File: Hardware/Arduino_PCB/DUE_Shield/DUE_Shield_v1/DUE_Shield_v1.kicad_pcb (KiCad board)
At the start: 2 copper layers, 101.6 x 62 mm, 34 parts, among them J1 SPI_Header, J2 Conn_02x05_Counter_Clockwise, J3 Reset_+_Dos, J4 V_Supply, J5 Main_Con, J6 Motor_PWM, J7 Audio, J8 Display_Con, J9 Erweiterungs_Con, P1 Digital, P2 Power, P3 Analog, P4 Analog, P5 PWM, P6 PWM, P7 Communication, U1 SD_Karte_Attend

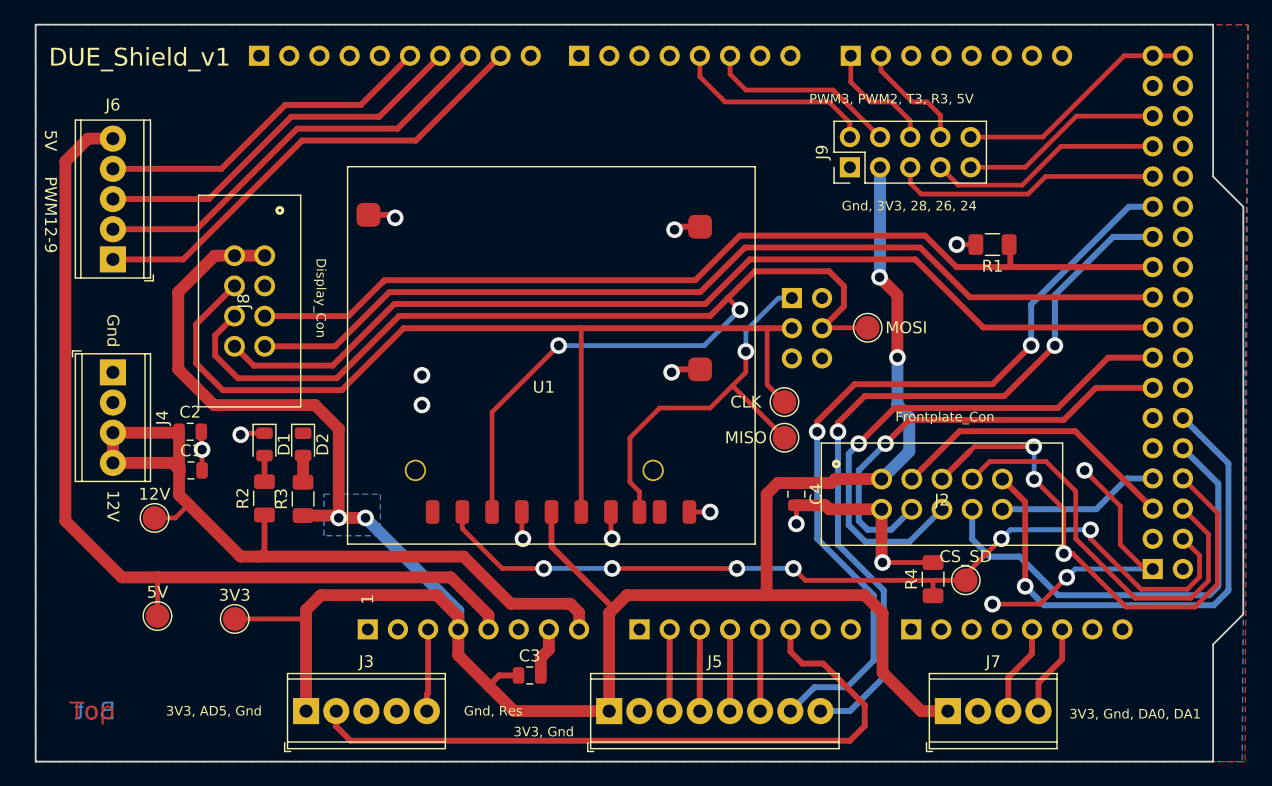
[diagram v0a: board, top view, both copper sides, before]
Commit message: Update DUE_Shield inkl. 3d-Modelle
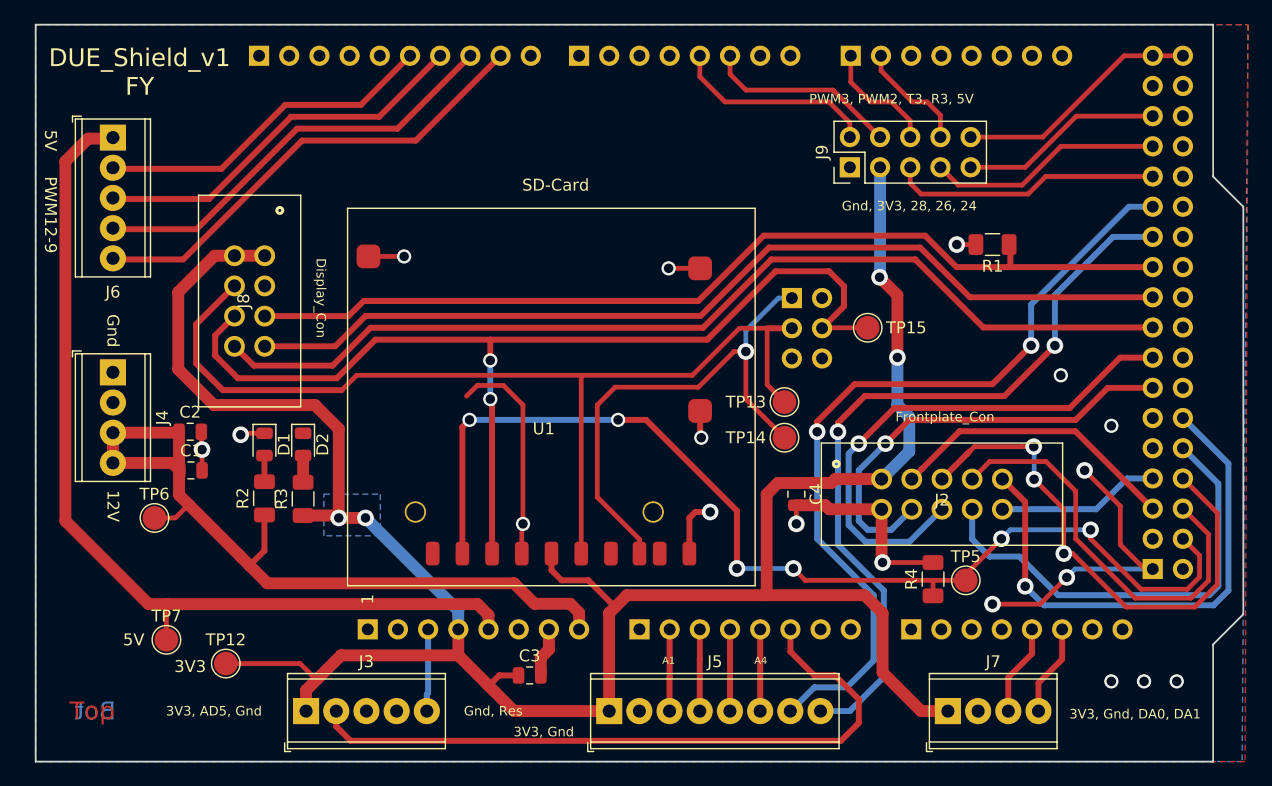
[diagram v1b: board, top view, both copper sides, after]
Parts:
- moved J6 10.2 mm to (109.9, 77.8), turned to 270 degrees
- moved TP12 3.82 mm to (119.4, 122.0)
- moved U1 3.50 mm to (146.1, 102.8)
- moved TP7 2.14 mm to (114.4, 120.0)
- renumbered 3V3 to TP12, CLK to TP13, MISO to TP14, MOSI to TP15, CS_SD to TP5, 12V to TP6, 5V to TP7
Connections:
- J6 pad 1: /9(**) -> +5V
- J6 pad 2: /10(**) -> /12(**)
- J6 pad 4: /12(**) -> /10(**)
- J6 pad 5: +5V -> /9(**)
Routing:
- net GND: track 67.9 -> 85.7 mm, vias 16 -> 18
- net /MOSI: track 104.3 -> 88.1 mm
- net /53: track 75.0 -> 91.1 mm
- net /MISO: track 33.3 -> 43.7 mm
- net +3V3: track 209.9 -> 201.6 mm
- net +12V: track 65.5 -> 66.6 mm
- net /A5: track 58.5 -> 57.7 mm
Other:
- board text added: "3V3"
- board text added: "A1"
- board text added: "A4"
- board text added: "DUE_Shield_v1 FY"
- board text added: "SD-Card"
- board text removed: "DUE_Shield_v1"
